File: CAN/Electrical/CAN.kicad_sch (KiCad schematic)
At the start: 32 parts, among them J1 Conn_01x05, P1 USB_C_Plug_USB2.0, SW1 Reset, U1 ESP32-C3-MINI-1, U2 AP2112K-3.3, U3 SN65HVD230, U5 FODM217D

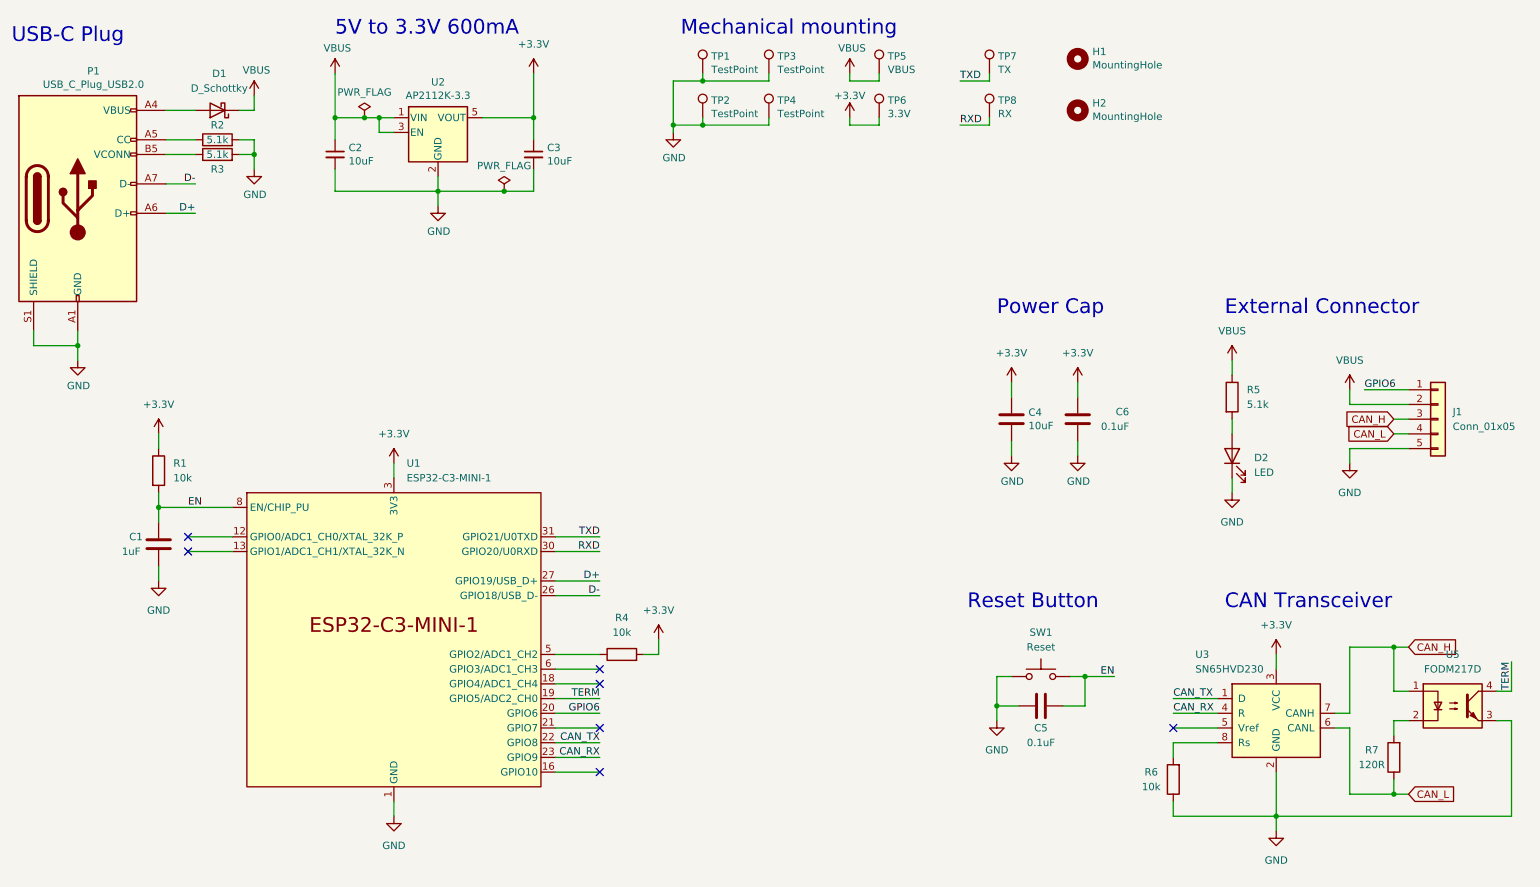
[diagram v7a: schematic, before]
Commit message: Added Resistor to protect optocoppler diode
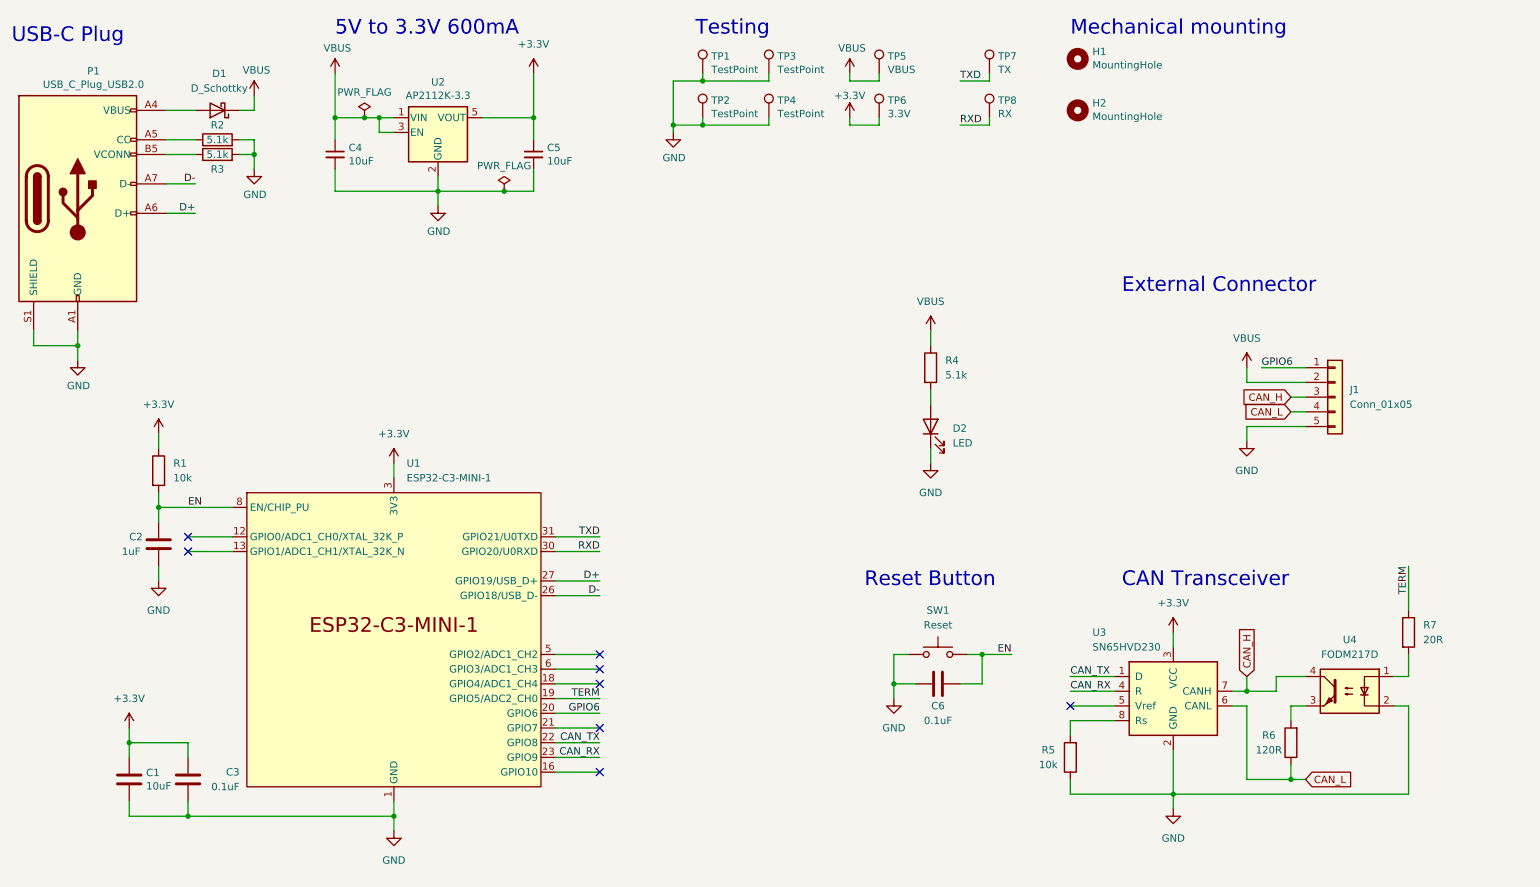
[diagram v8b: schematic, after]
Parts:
- removed C4: 10uF, Capacitor_SMD:C_0805_2012Metric_Pad1.18x1.45mm_HandSolder, symbol Device:C
- removed C6: 0.1uF, Capacitor_SMD:C_0805_2012Metric_Pad1.18x1.45mm_HandSolder, symbol Device:C
- removed R4: 10k, Resistor_SMD:R_0805_2012Metric_Pad1.20x1.40mm_HandSolder, symbol Device:R
- added C1: 10uF, Capacitor_SMD:C_0805_2012Metric_Pad1.18x1.45mm_HandSolder, symbol Device:C
- added C3: 0.1uF, Capacitor_SMD:C_0805_2012Metric_Pad1.18x1.45mm_HandSolder, symbol Device:C
- added R7: 20R, Resistor_SMD:R_0805_2012Metric_Pad1.20x1.40mm_HandSolder, symbol Device:R
- renumbered C1 to C2, C2 to C4, C3 to C5, C5 to C6, R5 to R4, R6 to R5, R7 to R6, U5 to U4
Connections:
- net +3.3V: now also C1.1, C3.2
- net CAN_H: now also U4.4; no longer U4.1
- net GND: now also U4.2, C1.2, C3.1; no longer U4.3
- net TERM: now also R7.1; no longer U4.4
- net at R6.2: now also U4.3; no longer U4.2
- new net: R7.2, U4.1
- no-connect marks 7 -> 8
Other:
- note added: "Testing"
- note removed: "Power Cap"
- moved on the sheet: C6, D2, J1, R4, R5, R6, SW1, U3, U4
